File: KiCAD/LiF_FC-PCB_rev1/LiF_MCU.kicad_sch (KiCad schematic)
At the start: 38 parts, among them J12 ESP 3V3_{EN}, J13 ESP_DGB_CONN, J14 CAN Upstream, J15 ESP_DGB_CONN, J16 ESP_DGB_CONN, Q1 MMBT4401, Q2 MMBT4401, SW1 Flash, SW2 Reset, U6 ESP32-S3-WROOM-1, U7 CY7C65213-28PVXI

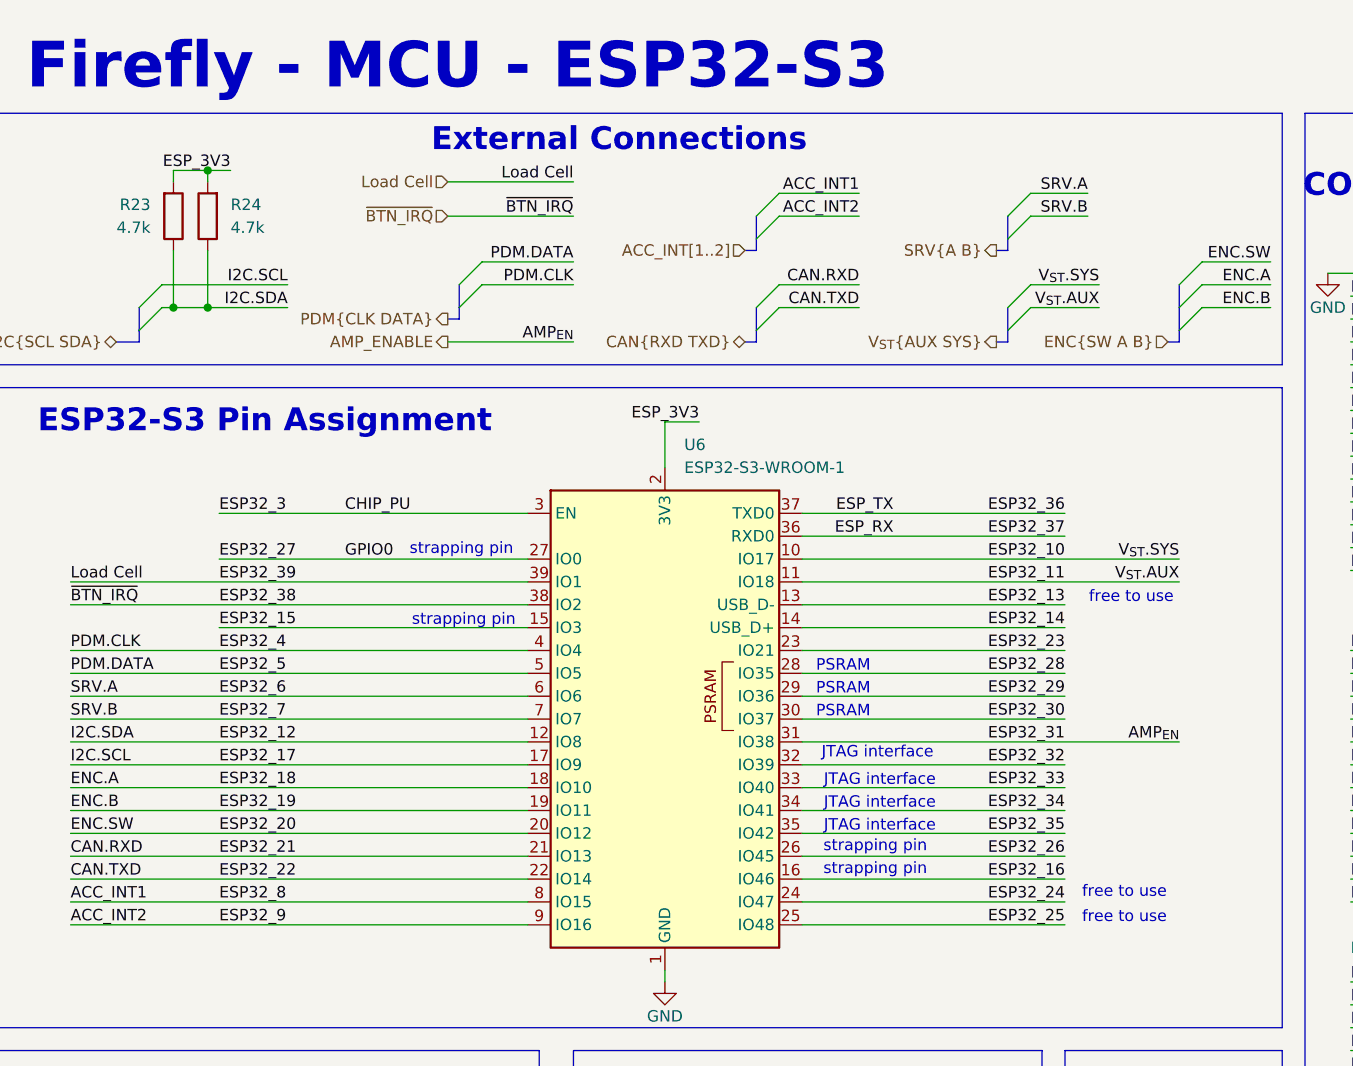
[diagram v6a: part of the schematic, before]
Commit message: added door limit switch and fixed I2C pull up resistors
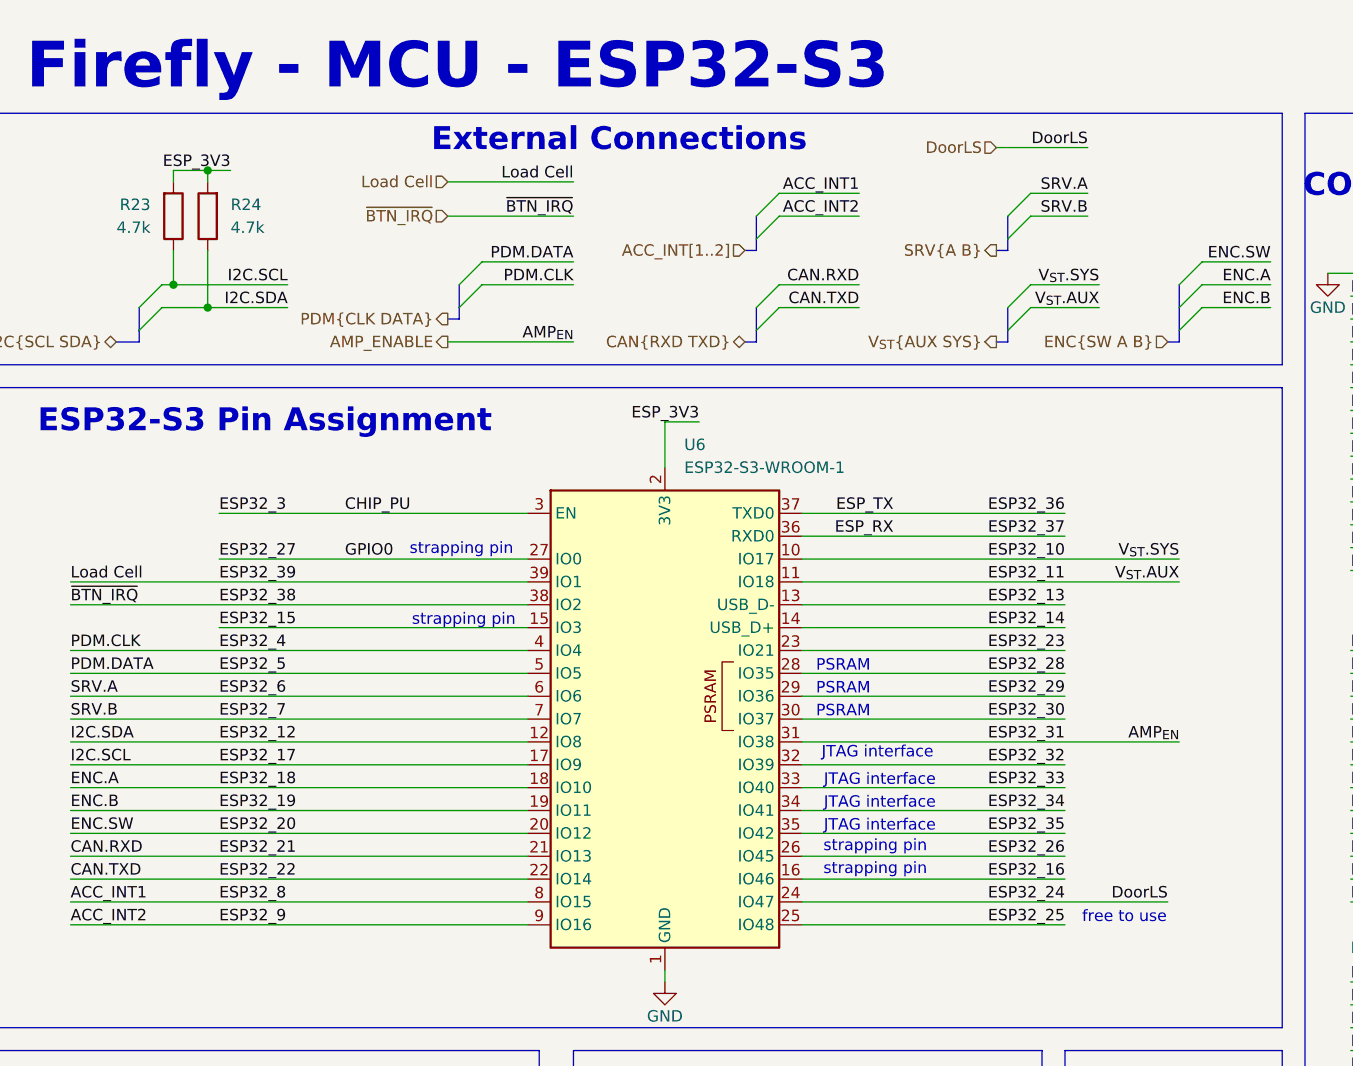
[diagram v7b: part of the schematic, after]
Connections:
- net ESP32_12: no longer R23.1
- net ESP32_17: now also R23.1
- net ESP32_24 renamed DoorLS
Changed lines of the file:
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@@
 		)
 	)
-	(text "free to use"
-		(exclude_from_sim no)
-		(at 237.744 109.474 0)
-		(effects
-			(font
-				(size 1.27 1.27)
-			)
-		)
-	)
 	(text "DEBUG\nCONNECTOR"
 		(exclude_from_sim no)
@@
 		)
 	)
-	(text "free to use"
-		(exclude_from_sim no)
-		(at 238.506 76.708 0)
-		(effects
-			(font
-				(size 1.27 1.27)
-			)
-		)
-	)
 	(text "JTAG interface"
 		(exclude_from_sim no)
@@
 	)
 	(junction
-		(at 132.08 44.45)
-		(diameter 0)
-		(color 0 0 0 0)
-	)
-	(junction
 		(at 86.36 85.09)
 		(diameter 0)
@@
 	)
 	(junction
+		(at 132.08 41.91)
+		(diameter 0)
+		(color 0 0 0 0)
+	)
+	(junction
 		(at 72.39 186.69)
 		(diameter 0)
@@
 	(wire
 		(pts
-			(xy 132.08 44.45) (xy 130.81 44.45)
+			(xy 130.81 44.45) (xy 135.89 44.45)
 		)
 		(stroke
@@
 	(wire
 		(pts
-			(xy 144.78 41.91) (xy 130.81 41.91)
+			(xy 144.78 41.91) (xy 132.08 41.91)
 		)
 		(stroke
@@
 	(wire
 		(pts
+			(xy 132.08 38.1) (xy 132.08 41.91)
+		)
+		(stroke
+			(width 0)
+			(type default)
+		)
+	)
+	(wire
+		(pts
 			(xy 219.71 144.78) (xy 219.71 147.32)
 		)
@@
 	(wire
 		(pts
-			(xy 132.08 38.1) (xy 132.08 44.45)
-		)
-		(stroke
-			(width 0)
-			(type default)
-		)
-	)
-	(wire
-		(pts
-			(xy 201.93 110.49) (xy 231.14 110.49)
+			(xy 201.93 110.49) (xy 242.57 110.49)
 		)
 		(stroke
@@
 	(wire
 		(pts
+			(xy 132.08 41.91) (xy 130.81 41.91)
+		)
+		(stroke
+			(width 0)
+			(type default)
+		)
+	)
+	(wire
+		(pts
 			(xy 49.53 152.4) (xy 57.15 152.4)
 		)
@@
 		)
 	)
-	(wire
-		(pts
-			(xy 135.89 44.45) (xy 132.08 44.45)
-		)
-		(stroke
-			(width 0)
-			(type default)
-		)
-	)
 	(bus
 		(pts
@@
 	(wire
 		(pts
+			(xy 223.52 26.67) (xy 233.68 26.67)
+		)
+		(stroke
+			(width 0)
+			(type default)
+		)
+	)
+	(wire
+		(pts
 			(xy 207.01 144.78) (xy 209.55 144.78)
 		)
@@
 		)
 	)
+	(label "DoorLS"
+		(at 242.57 110.49 180)
+		(effects
+			(font
+				(size 1.27 1.27)
+			)
+			(justify right bottom)
+		)
+	)
 	(label "ESP32_10"
 		(at 231.14 72.39 180)
@@
 		)
 	)
+	(label "DoorLS"
+		(at 233.68 26.67 180)
+		(effects
+			(font
+				(size 1.27 1.27)
+			)
+			(justify right bottom)
+		)
+	)
 	(label "CAN.TXD"
 		(at 208.28 44.45 180)
@@
 		(effects
 			(font
+				(size 1.27 1.27)
+			)
+			(justify right)
+		)
+	)
+	(hierarchical_label "DoorLS"
+		(shape input)
+		(at 223.52 26.67 180)
+		(effects
+			(font

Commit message: backup before expanding the board size
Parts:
- SW1, SW2: footprint LiF_PCB_Footprints:SW_TL3301PF160QG -> LiF_PCB_Footprints:SON4_PTS526 SM15 SMTR2 LFS_CNK; DKPN EG4562CT-ND -> CKN12220-1-ND; MANUFACTURER E-Switch -> (none); MAXIMUM_PACKAGE_HEIGHT 5 mm -> (none); PARTREV E -> (none); PN TL3301PF160QG -> PTS526SM15SMTR2 LFS; SNAPEDA_PN TL3301AF160QG -> (none); STANDARD Manufacturer Recommendations -> (none)
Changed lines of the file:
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@@
-	)
-	(symbol
-		(lib_id "LiF_PCB_Symbols:TL3301PF160QG")
-		(at 208.28 151.13 90)
-		(mirror x)
-		(unit 1)
-		(exclude_from_sim no)
-		(in_bom yes)
-		(on_board yes)
-		(dnp no)
-		(property "Reference" "SW2"
-			(at 215.646 149.86 90)
-			(effects
-				(font
-					(size 1.27 1.27)
-				)
-				(justify left)
-			)
-		)
-		(property "Value" "Reset"
-			(at 215.646 151.892 90)
-			(effects
-				(font
-					(size 1.27 1.27)
-				)
-				(justify left)
-			)
-		)
-		(property "Footprint" "LiF_PCB_Footprints:SW_TL3301PF160QG"
-			(at 196.596 150.114 0)
-			(effects
-				(font
-					(size 1.27 1.27)
-				)
-				(justify bottom)
-				(hide yes)
-			)
-		)
-		(property "Datasheet" "https://configured-product-images.s3.amazonaws.com/Datasheets/TL3301.pdf"
-			(at 200.406 149.098 0)
-			(effects
-				(font
-					(size 1.27 1.27)
-				)
-				(hide yes)
-			)
-		)
-		(property "Description" "Tactile Switch SPST-NO Top Actuated Surface Mount"
-			(at 200.406 149.098 0)
-			(effects
-				(font
-					(size 1.27 1.27)
-				)
-				(hide yes)
-			)
-		)
-		(property "PARTREV" "E"
-			(at 192.532 151.13 0)
-			(effects
-				(font
-					(size 1.27 1.27)
-				)
-				(justify bottom)
-				(hide yes)
-			)
-		)
-		(property "STANDARD" "Manufacturer Recommendations"
-			(at 196.596 150.114 0)
-			(effects
-				(font
-					(size 1.27 1.27)
-				)
-				(justify bottom)
-				(hide yes)
-			)
-		)
-		(property "MANUFACTURER" "E-Switch"
-			(at 194.31 151.384 0)
-			(effects
-				(font
-					(size 1.27 1.27)
-				)
-				(justify bottom)
-				(hide yes)
-			)
-		)
-		(property "MAXIMUM_PACKAGE_HEIGHT" "5 mm"
-			(at 192.532 151.13 0)
-			(effects
-				(font
-					(size 1.27 1.27)
-				)
-				(justify bottom)
-				(hide yes)
-			)
-		)
-		(property "SNAPEDA_PN" "TL3301AF160QG"
-			(at 194.31 151.384 0)
-			(effects
-				(font
-					(size 1.27 1.27)
-				)
-				(justify bottom)
-				(hide yes)
-			)
-		)
-		(property "PN" "TL3301PF160QG"
-			(at 199.644 150.622 0)
-			(effects
-				(font
-					(size 1.27 1.27)
-				)
-				(hide yes)
-			)
-		)
-		(property "DKPN" "EG4562CT-ND"
-			(at 199.644 150.622 0)
-			(effects
-				(font
-					(size 1.27 1.27)
-				)
-				(hide yes)
-			)
-		)
-		(pin "3"
-		)
-		(pin "4"
-		)
-		(pin "1"
-		)
-		(pin "2"
-		)
-		(instances
-			(project "LiF_FC-PCB_rev1"
-				(path "/9e3e8da7-e506-46c9-90e5-307e4ad30d29/fa6eb845-b5e3-4a8e-9c24-c1b567f4e987"
-					(reference "SW2")
-					(unit 1)
-				)
-			)
-		)
 	)
 	(symbol
@@
 			)
 		)
-		(property "Footprint" "LiF_PCB_Footprints:SW_TL3301PF160QG"
+		(property "Footprint" "LiF_PCB_Footprints:SON4_PTS526 SM15 SMTR2 LFS_CNK"
 			(at 171.196 148.844 0)
 			(effects
@@
 			)
 		)
-		(property "PARTREV" "E"
-			(at 167.132 149.86 0)
-			(effects
-				(font
-					(size 1.27 1.27)
-				)
-				(justify bottom)
-				(hide yes)
-			)
-		)
-		(property "STANDARD" "Manufacturer Recommendations"
-			(at 171.196 148.844 0)
-			(effects
-				(font
-					(size 1.27 1.27)
-				)
-				(justify bottom)
-				(hide yes)
-			)
-		)
-		(property "MANUFACTURER" "E-Switch"
-			(at 168.91 150.114 0)
-			(effects
-				(font
-					(size 1.27 1.27)
-				)
-				(justify bottom)
-				(hide yes)
-			)
-		)
-		(property "MAXIMUM_PACKAGE_HEIGHT" "5 mm"
-			(at 167.132 149.86 0)
-			(effects
-				(font
-					(size 1.27 1.27)
-				)
-				(justify bottom)
-				(hide yes)
-			)
-		)
-		(property "SNAPEDA_PN" "TL3301AF160QG"
-			(at 168.91 150.114 0)
-			(effects
-				(font
-					(size 1.27 1.27)
-				)
-				(justify bottom)
-				(hide yes)
-			)
-		)
-		(property "PN" "TL3301PF160QG"
+		(property "PN" "PTS526SM15SMTR2 LFS"
 			(at 174.244 149.352 0)
 			(effects
@@
 			)
 		)
-		(property "DKPN" "EG4562CT-ND"
+		(property "DKPN" "CKN12220-1-ND"
 			(at 174.244 149.352 0)
 			(effects
@@
 					(unit 1)
 				)
+			)
+		)
+	)
+	(symbol
+		(lib_id "LiF_PCB_Symbols:TL3301PF160QG")
+		(at 208.28 151.13 90)
+		(mirror x)
+		(unit 1)
+		(exclude_from_sim no)
+		(in_bom yes)
+		(on_board yes)
+		(dnp no)
+		(property "Reference" "SW2"
+			(at 215.646 149.86 90)
+			(effects
+				(font
+					(size 1.27 1.27)
+				)
+				(justify left)
+			)
+		)
+		(property "Value" "Reset"
+			(at 215.646 151.892 90)
+			(effects
+				(font
+					(size 1.27 1.27)
+				)
+				(justify left)
+			)
+		)
+		(property "Footprint" "LiF_PCB_Footprints:SON4_PTS526 SM15 SMTR2 LFS_CNK"
+			(at 196.596 150.114 0)
+			(effects
+				(font
+					(size 1.27 1.27)
+				)
+				(justify bottom)
+				(hide yes)
+			)
+		)
+		(property "Datasheet" "https://configured-product-images.s3.amazonaws.com/Datasheets/TL3301.pdf"
+			(at 200.406 149.098 0)
+			(effects
+				(font
+					(size 1.27 1.27)
+				)
+				(hide yes)
+			)
+		)
+		(property "Description" "Tactile Switch SPST-NO Top Actuated Surface Mount"
+			(at 200.406 149.098 0)
+			(effects
+				(font
+					(size 1.27 1.27)
+				)
+				(hide yes)
+			)
+		)
+		(property "PN" "PTS526SM15SMTR2 LFS"
+			(at 199.644 150.622 0)
+			(effects
+				(font
+					(size 1.27 1.27)
+				)
+				(hide yes)
+			)
+		)
+		(property "DKPN" "CKN12220-1-ND"
+			(at 199.644 150.622 0)
+			(effects
+				(font
+					(size 1.27 1.27)
+				)
+				(hide yes)
+			)
+		)
+		(pin "3"
+		)
+		(pin "4"
+		)
+		(pin "1"
+		)
+		(pin "2"
+		)
+		(instances
+			(project "LiF_FC-PCB_rev1"
+				(path "/9e3e8da7-e506-46c9-90e5-307e4ad30d29/fa6eb845-b5e3-4a8e-9c24-c1b567f4e987"
+					(reference "SW2")
+					(unit 1)
+				)
